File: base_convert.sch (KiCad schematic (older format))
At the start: 15 parts, among them J1 ISP, J2 DEBUG, J3 Vin, Q1 Q_PMOS_GSD, SW1 SELECT, U1 MIC5317-3.3YM5-TR, U2 MSP430FR2033IPMR

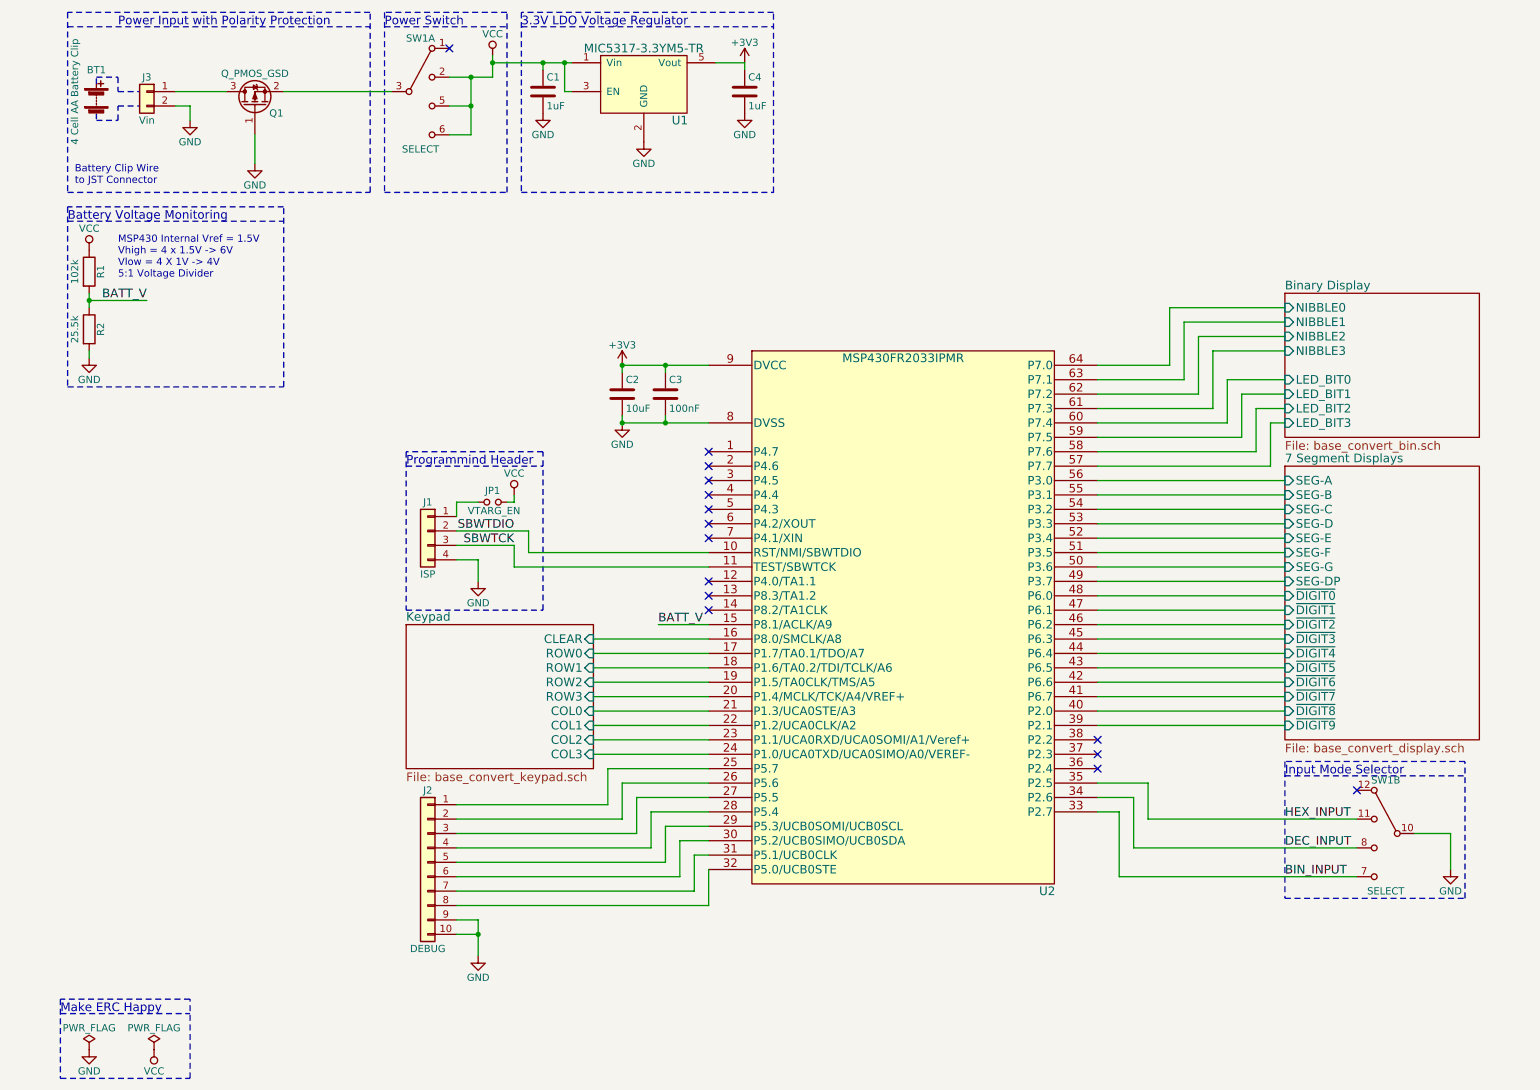
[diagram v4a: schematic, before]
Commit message: remove extra gpio header
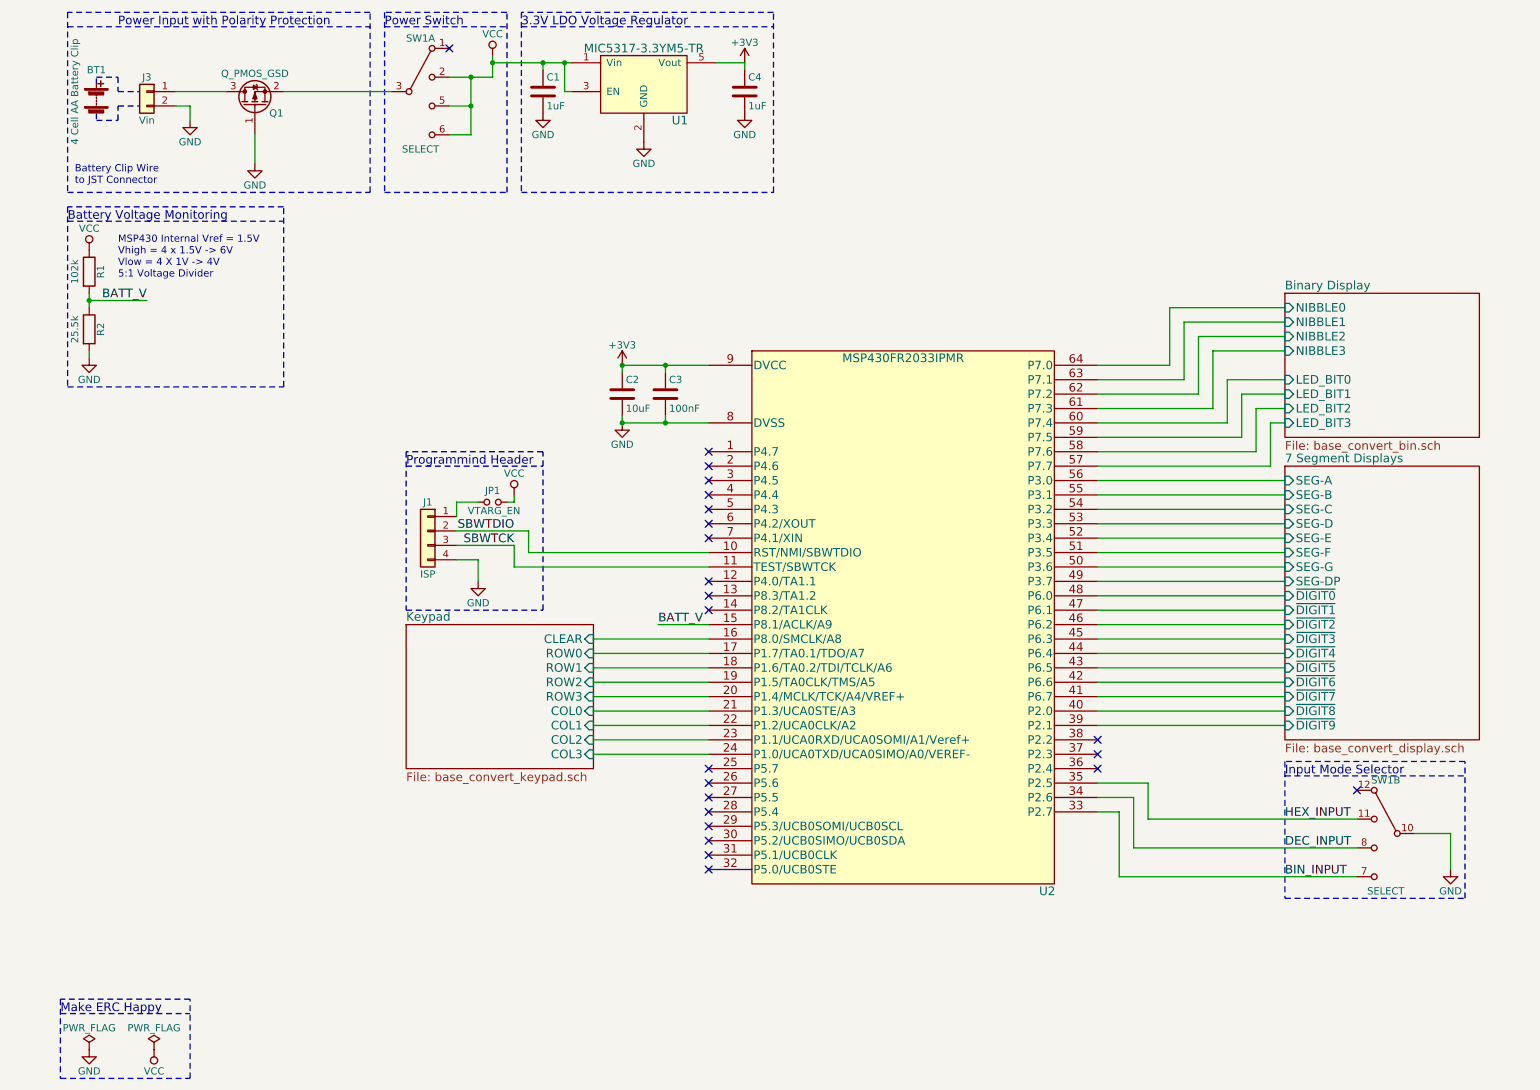
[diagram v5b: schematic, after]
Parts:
- removed J2: DEBUG, Pin_Headers:Pin_Header_Straight_1x10_Pitch2.54mm, symbol Conn_01x10
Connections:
- no-connect marks 15 -> 23
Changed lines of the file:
@@
-$EndComp
-$Comp
-L Conn_01x10 J2
-U 1 1 5B285C9A
-P 3100 6450
-F 0 "J2" H 3100 6950 50  0000 C CNN
-F 1 "DEBUG" H 3100 5850 50  0000 C CNN
-F 2 "Pin_Headers:Pin_Header_Straight_1x10_Pitch2.54mm" H 3100 6450 50  0001 C CNN
-F 3 "" H 3100 6450 50  0001 C CNN
-	1    3100 6450
-	-1   0    0    -1
-$EndComp
-$Comp
-L GND #PWR015
-U 1 1 5B2882B1
-P 3450 7100
-F 0 "#PWR015" H 3450 6850 50  0001 C CNN
-F 1 "GND" H 3450 6950 50  0000 C CNN
-F 2 "" H 3450 7100 50  0001 C CNN
-F 3 "" H 3450 7100 50  0001 C CNN
-	1    3450 7100
-	1    0    0    -1
 $EndComp
 $Comp
@@
 	1900 1600 1900 1400
 Wire Wire Line
-	4450 3000 4750 3000
-Wire Wire Line
-	4750 3000 5050 3000
+	4450 3000 5050 3000
 Wire Wire Line
 	4450 3000 4450 3050
@@
 	4450 3350 4450 3400
 Wire Wire Line
-	4450 3400 4750 3400
-Wire Wire Line
-	4750 3400 5050 3400
+	4450 3400 5050 3400
 Wire Wire Line
 	3400 1400 3250 1400
@@
 	750  2950 750  2900
 Wire Wire Line
-	750  2500 750  2550
-Wire Wire Line
-	750  2550 750  2600
+	750  2500 750  2600
 Wire Wire Line
 	750  2550 1150 2550
@@
 	5300 900  5300 950
 Wire Wire Line
-	3400 1000 3400 1200
-Wire Wire Line
-	3400 1200 3400 1400
+	3400 1000 3400 1400
 Wire Wire Line
 	3300 4050 3300 3950
@@
 	2950 3700 3900 3700
 Wire Wire Line
-	3550 1000 3400 1000
-Wire Wire Line
-	3400 1000 3250 1000
-Wire Wire Line
-	3550 900  3900 900
-Wire Wire Line
-	3900 900  4050 900
-Wire Wire Line
-	4050 900  4100 900
+	3550 1000 3250 1000
+Wire Wire Line
+	3550 900  4100 900
 Wire Notes Line
 	3750 550  3750 1800
@@
 	2800 650  3650 650
 Wire Wire Line
-	3550 850  3550 900
-Wire Wire Line
-	3550 900  3550 1000
+	3550 850  3550 1000
 Wire Wire Line
 	4750 3400 4750 3350
@@
 Wire Wire Line
 	4700 4800 5050 4800
-Wire Wire Line
-	3300 6050 4350 6050
-Wire Wire Line
-	4350 6050 4350 5800
-Wire Wire Line
-	4350 5800 5050 5800
-Wire Wire Line
-	3300 6150 4450 6150
-Wire Wire Line
-	4450 6150 4450 5900
-Wire Wire Line
-	4450 5900 5050 5900
-Wire Wire Line
-	5050 6000 4550 6000
-Wire Wire Line
-	4550 6000 4550 6250
-Wire Wire Line
-	4550 6250 3300 6250
-Wire Wire Line
-	3300 6350 4650 6350
-Wire Wire Line
-	4650 6350 4650 6100
-Wire Wire Line
-	4650 6100 5050 6100
-Wire Wire Line
-	5050 6200 4750 6200
-Wire Wire Line
-	4750 6200 4750 6450
-Wire Wire Line
-	4750 6450 3300 6450
-Wire Wire Line
-	3300 6550 4850 6550
-Wire Wire Line
-	4850 6550 4850 6300
-Wire Wire Line
-	4850 6300 5050 6300
-Wire Wire Line
-	5050 6400 4950 6400
-Wire Wire Line
-	4950 6400 4950 6650
-Wire Wire Line
-	4950 6650 3300 6650
-Wire Wire Line
-	3300 6750 5050 6750
-Wire Wire Line
-	5050 6750 5050 6500
-Wire Wire Line
-	3450 6850 3450 6950
-Wire Wire Line
-	3450 6950 3450 7100
-Wire Wire Line
-	3450 6850 3300 6850
-Wire Wire Line
-	3300 6950 3450 6950
 Connection ~ 4750 3000
 Connection ~ 4750 3400
@@
 Connection ~ 3550 900
 Connection ~ 4450 3400
-Connection ~ 3450 6950
 NoConn ~ 3250 800
 NoConn ~ 9550 5950
@@
 	1    0    0    -1
 $EndComp
+NoConn ~ 5050 5800
+NoConn ~ 5050 5900
+NoConn ~ 5050 6000
+NoConn ~ 5050 6100
+NoConn ~ 5050 6200
+NoConn ~ 5050 6300
+NoConn ~ 5050 6400
+NoConn ~ 5050 6500
 $EndSCHEMATC

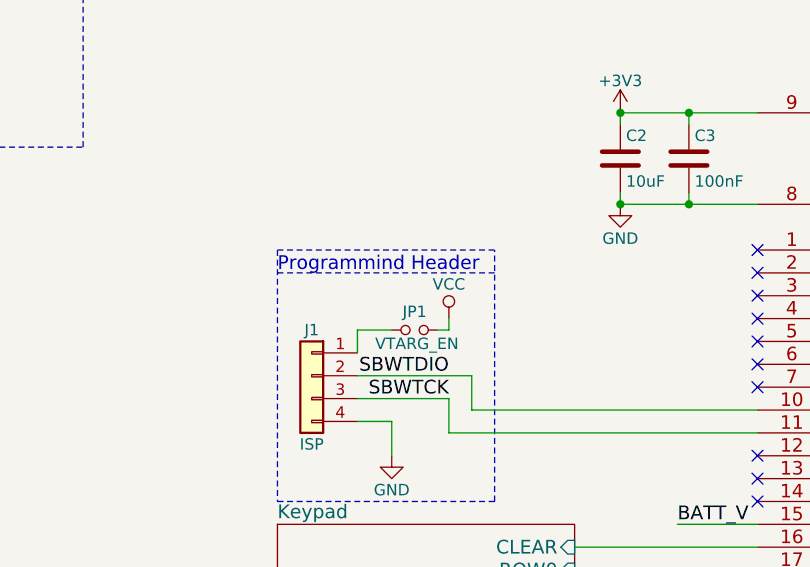
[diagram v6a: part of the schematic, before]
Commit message: Vtarg connect to 3v3 not Vcc
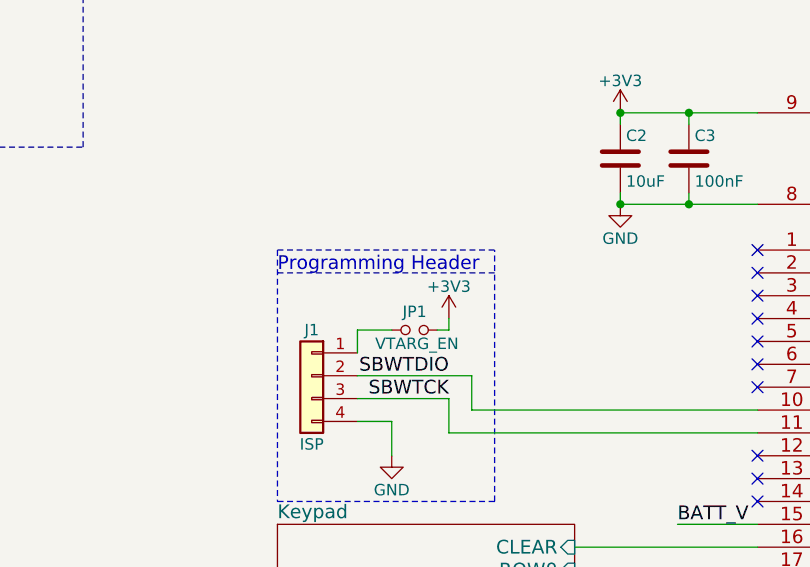
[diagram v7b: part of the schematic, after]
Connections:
- net +3V3: now also JP1.2
- net VCC: no longer JP1.2
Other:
- note added: "Programming Header"
- note removed: "Programmind Header"
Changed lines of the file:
@@
-$EndComp
-$Comp
-L VCC #PWR07
-U 1 1 5AF43264
-P 3700 3900
-F 0 "#PWR07" H 3700 3750 50  0001 C CNN
-F 1 "VCC" H 3700 4050 50  0000 C CNN
-F 2 "" H 3700 3900 50  0001 C CNN
-F 3 "" H 3700 3900 50  0001 C CNN
-	1    3700 3900
-	1    0    0    -1
 $EndComp
 $Comp
@@
 $EndComp
 $Comp
-L GND #PWR08
+L GND #PWR07
 U 1 1 5B285DA8
 P 3900 1250
-F 0 "#PWR08" H 3900 1000 50  0001 C CNN
+F 0 "#PWR07" H 3900 1000 50  0001 C CNN
 F 1 "GND" H 3900 1100 50  0000 C CNN
 F 2 "" H 3900 1250 50  0001 C CNN
@@
 $EndComp
 $Comp
-L GND #PWR09
+L GND #PWR08
 U 1 1 5B285FB6
 P 4600 1450
-F 0 "#PWR09" H 4600 1200 50  0001 C CNN
+F 0 "#PWR08" H 4600 1200 50  0001 C CNN
 F 1 "GND" H 4600 1300 50  0000 C CNN
 F 2 "" H 4600 1450 50  0001 C CNN
@@
 $EndComp
 $Comp
-L GND #PWR010
+L GND #PWR09
 U 1 1 5B286569
 P 5300 1250
-F 0 "#PWR010" H 5300 1000 50  0001 C CNN
+F 0 "#PWR09" H 5300 1000 50  0001 C CNN
 F 1 "GND" H 5300 1100 50  0000 C CNN
 F 2 "" H 5300 1250 50  0001 C CNN
@@
 $EndComp
 $Comp
-L VCC #PWR011
+L VCC #PWR010
 U 1 1 5B28B1DA
 P 750 2200
-F 0 "#PWR011" H 750 2050 50  0001 C CNN
+F 0 "#PWR010" H 750 2050 50  0001 C CNN
 F 1 "VCC" H 750 2350 50  0000 C CNN
 F 2 "" H 750 2200 50  0001 C CNN
@@
 $EndComp
 $Comp
-L +3V3 #PWR012
+L +3V3 #PWR011
 U 1 1 5B28D631
 P 5300 900
-F 0 "#PWR012" H 5300 750 50  0001 C CNN
+F 0 "#PWR011" H 5300 750 50  0001 C CNN
 F 1 "+3V3" H 5300 1040 50  0000 C CNN
 F 2 "" H 5300 900 50  0001 C CNN
@@
 $EndComp
 $Comp
-L VCC #PWR013
+L VCC #PWR012
 U 1 1 5B29E8A8
 P 3550 850
-F 0 "#PWR013" H 3550 700 50  0001 C CNN
+F 0 "#PWR012" H 3550 700 50  0001 C CNN
 F 1 "VCC" H 3550 1000 50  0000 C CNN
 F 2 "" H 3550 850 50  0001 C CNN
@@
 $EndComp
 $Comp
-L +3V3 #PWR014
+L +3V3 #PWR013
 U 1 1 5B2A0C6B
 P 4450 3000
-F 0 "#PWR014" H 4450 2850 50  0001 C CNN
+F 0 "#PWR013" H 4450 2850 50  0001 C CNN
 F 1 "+3V3" H 4450 3140 50  0000 C CNN
 F 2 "" H 4450 3000 50  0001 C CNN
@@
 $EndComp
 $Comp
-L PWR_FLAG #FLG016
+L PWR_FLAG #FLG014
 U 1 1 5B2BCABB
 P 750 7750
-F 0 "#FLG016" H 750 7825 50  0001 C CNN
+F 0 "#FLG014" H 750 7825 50  0001 C CNN
 F 1 "PWR_FLAG" H 750 7900 50  0000 C CNN
 F 2 "" H 750 7750 50  0001 C CNN
@@
 $EndComp
 $Comp
-L GND #PWR017
+L GND #PWR015
 U 1 1 5B2BCBCF
 P 750 7750
-F 0 "#PWR017" H 750 7500 50  0001 C CNN
+F 0 "#PWR015" H 750 7500 50  0001 C CNN
 F 1 "GND" H 750 7600 50  0000 C CNN
 F 2 "" H 750 7750 50  0001 C CNN
@@
 $EndComp
 $Comp
-L VCC #PWR018
+L VCC #PWR016
 U 1 1 5B2C495B
 P 1200 7750
-F 0 "#PWR018" H 1200 7600 50  0001 C CNN
+F 0 "#PWR016" H 1200 7600 50  0001 C CNN
 F 1 "VCC" H 1200 7900 50  0000 C CNN
 F 2 "" H 1200 7750 50  0001 C CNN
@@
 $EndComp
 $Comp
-L PWR_FLAG #FLG019
+L PWR_FLAG #FLG017
 U 1 1 5B2C4DB7
 P 1200 7750
-F 0 "#FLG019" H 1200 7825 50  0001 C CNN
+F 0 "#FLG017" H 1200 7825 50  0001 C CNN
 F 1 "PWR_FLAG" H 1200 7900 50  0000 C CNN
 F 2 "" H 1200 7750 50  0001 C CNN
@@
 SBWTCK
 Text Notes 2950 3700 0    60   ~ 0
-Programmind Header
+Programming Header
 Text Notes 3750 650  0    60   ~ 0
 3.3V LDO Voltage Regulator
@@
 NoConn ~ 5050 6400
 NoConn ~ 5050 6500
+$Comp
+L +3V3 #PWR018
+U 1 1 5B340006
+P 3700 3900
+F 0 "#PWR018" H 3700 3750 50  0001 C CNN
+F 1 "+3V3" H 3700 4040 50  0000 C CNN
+F 2 "" H 3700 3900 50  0001 C CNN
+F 3 "" H 3700 3900 50  0001 C CNN
+	1    3700 3900
+	1    0    0    -1
+$EndComp
 $EndSCHEMATC
